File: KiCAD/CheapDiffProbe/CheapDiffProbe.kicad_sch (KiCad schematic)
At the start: 41 parts, among them U1 TL072, U2 TL072

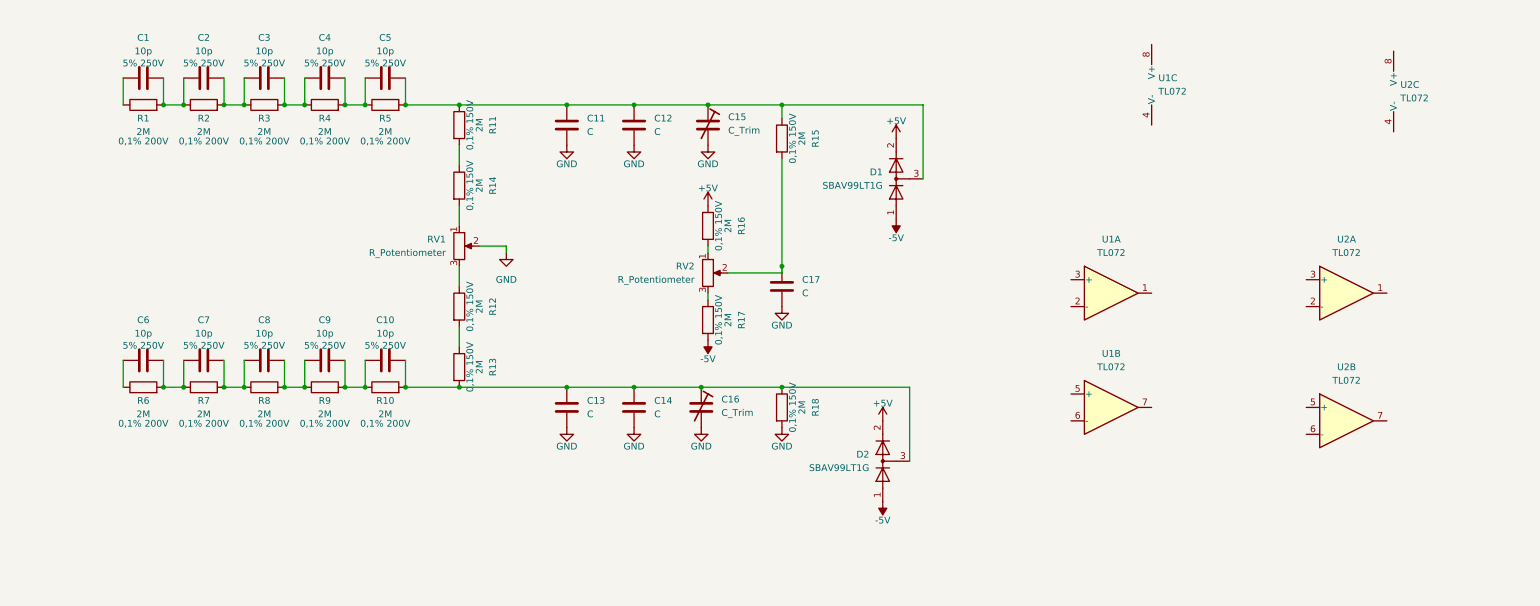
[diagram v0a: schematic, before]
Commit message: Updated schematic, values needs to be calculated
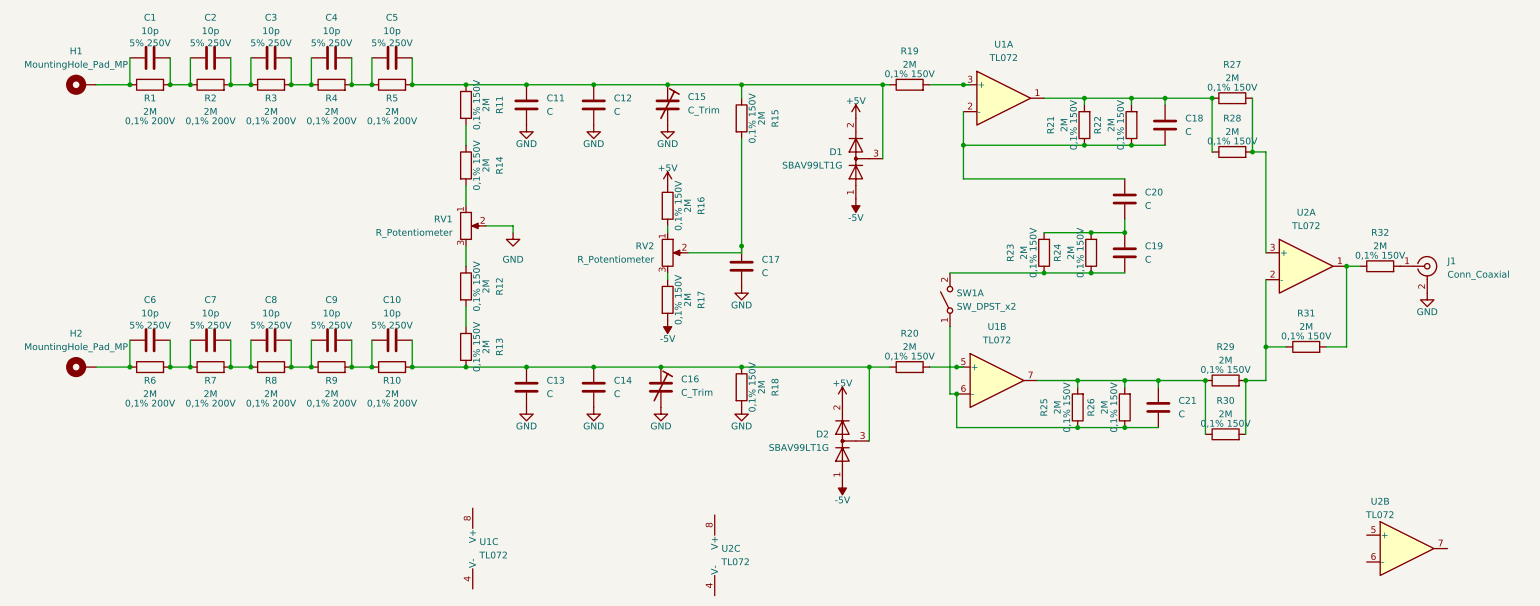
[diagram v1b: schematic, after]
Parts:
- added C18, C19, C20, C21: C, symbol Device:C
- added H1, H2: MountingHole_Pad_MP, symbol Mechanical:MountingHole_Pad_MP
- added J1: Conn_Coaxial, symbol Connector:Conn_Coaxial
- added R19, R20, R21, R22, R23, R24, R25, R26, R27, R28, R29, R30, R31, R32: 2M, Capacitor_SMD:C_0805_2012Metric_Pad1.18x1.45mm_HandSolder, symbol Device:R
- added SW1: SW_DPST_x2, symbol Switch:SW_DPST_x2
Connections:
- net GND: now also J1.2 (Ext)
- net at U2.1: now also R31.2, R32.1
- net at U2.2 (-): now also R29.2, R30.2, R31.1
- net at U2.3 (+): now also R27.2, R28.2
- net at C11.1, C12.1, C15.1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: now also R19.1
- net at C10.2, C13.1, C14.1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: now also R20.1
- net at C1.1, R1.1: now also H1.MP
- net at U1.1: now also C18.1, R21.2, R22.2, R27.1, R28.1
- net at U1.2 (-): now also C18.2, C20.1, R21.1, R22.1
- net at U1.3 (+): now also R19.2
- net at C6.1, R6.1: now also H2.MP
- net at U1.5 (+): now also R20.2
- net at U1.6 (-): now also C21.2, R25.1, R26.1, SW1.1 (A)
- net at U1.7: now also C21.1, R25.2, R26.2, R29.1, R30.1
- new net: C19.1, C20.2, R23.2, R24.2
- new net: J1.1 (In), R32.2
- new net: C19.2, R23.1, R24.1, SW1.2 (B)
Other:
- moved on the sheet: C1, C10, C11, C12, C13, C14, C15, C16, C17, C2, C3, C4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
